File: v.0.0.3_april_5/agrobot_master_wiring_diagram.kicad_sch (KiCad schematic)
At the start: 221 parts

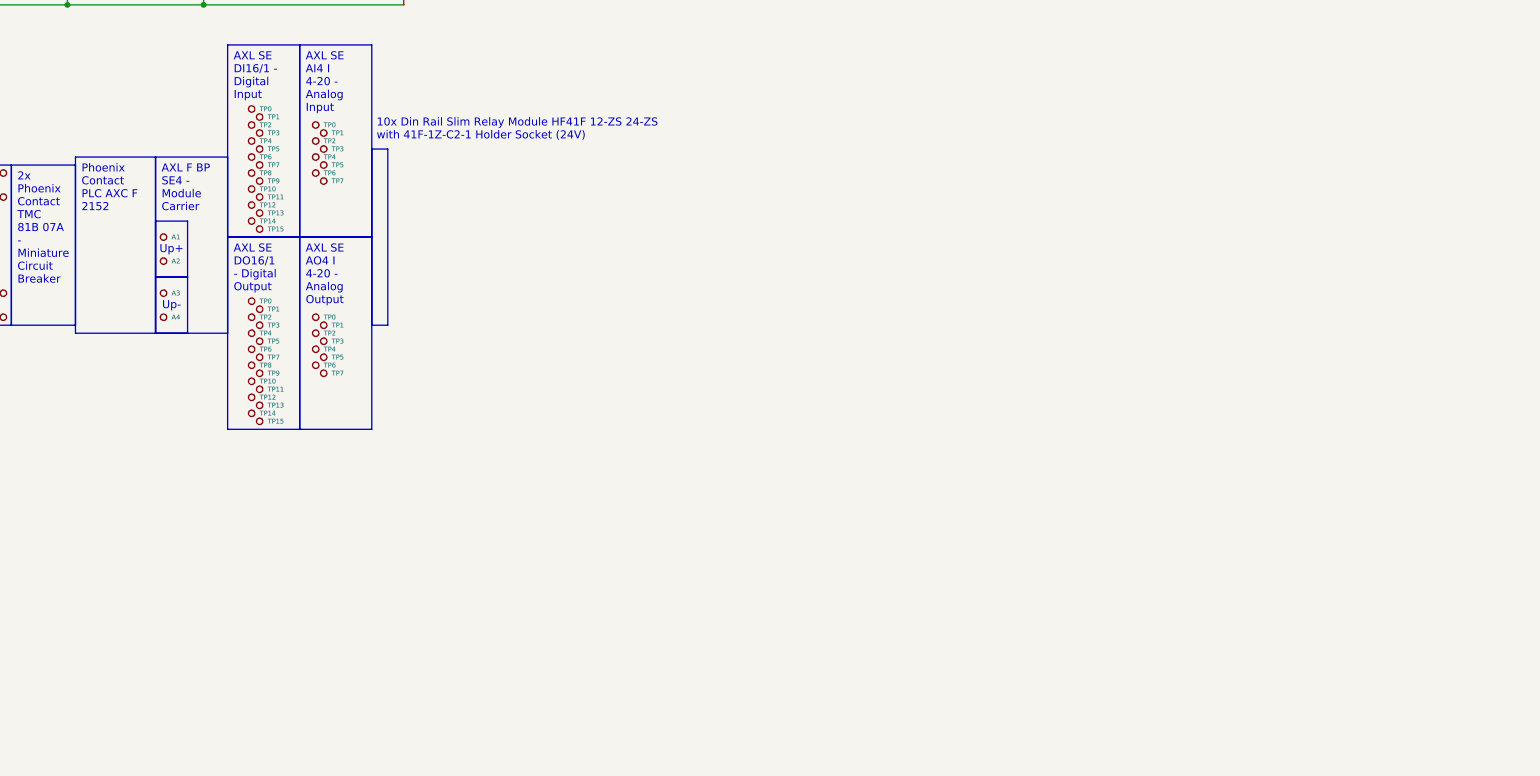
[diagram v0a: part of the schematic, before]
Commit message: Added Relays and LED Tower
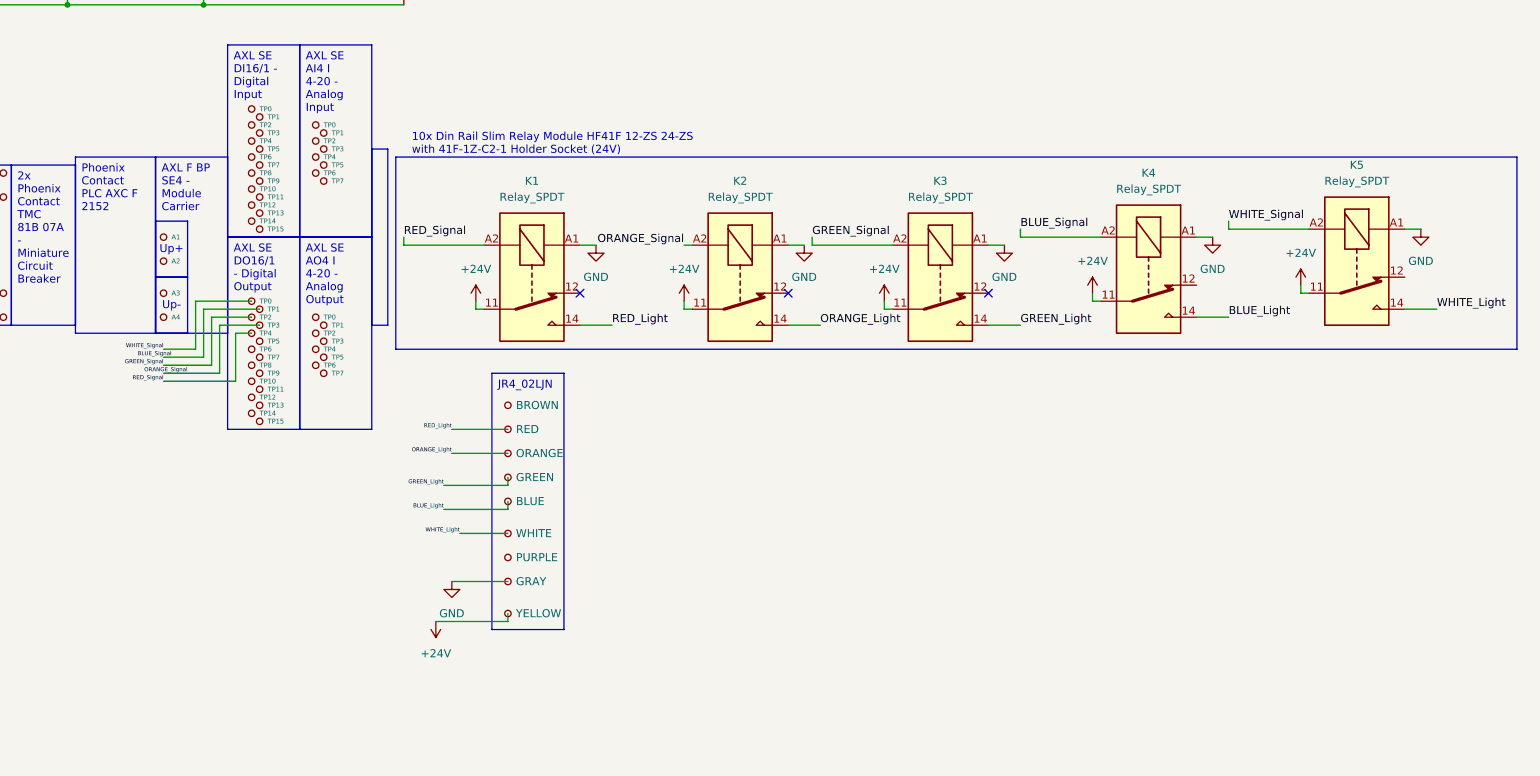
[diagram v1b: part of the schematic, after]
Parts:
- added BLUE, BROWN, GRAY, GREEN, ORANGE, PURPLE, RED, WHITE, YELLOW: (no value), symbol Connector:TestPoint_Small
- added K1, K2, K3, K4, K5: Relay_SPDT, symbol Relay:Relay_SPDT
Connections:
- net +24V: now also K1.11, K2.11, K3.11, K4.11, K5.11, YELLOW.1
- net GND: now also GRAY.1, K1.A1, K2.A1, K3.A1, K4.A1, K5.A1
- net RED_Signal: now reaches TP4.1
- net RED_Signal: now also K1.A2
- net ORANGE_Signal: now reaches TP3.1
- net ORANGE_Signal: now also K2.A2
- net BLUE_Signal: now reaches TP1.1
- net BLUE_Signal: now also K4.A2
- net WHITE_Signal: now reaches TP0.1
- net WHITE_Signal: now also K5.A2
- net GREEN_Signal: now reaches TP2.1
- net GREEN_Signal: now also K3.A2
- new net BLUE_Light: BLUE.1, K4.14
- new net GREEN_Light: GREEN.1, K3.14
- new net ORANGE_Light: K2.14, ORANGE.1
- new net RED_Light: K1.14, RED.1
- new net WHITE_Light: K5.14, WHITE.1
- no-connect marks 0 -> 3
